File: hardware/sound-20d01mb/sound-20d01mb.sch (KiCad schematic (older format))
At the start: 6 parts

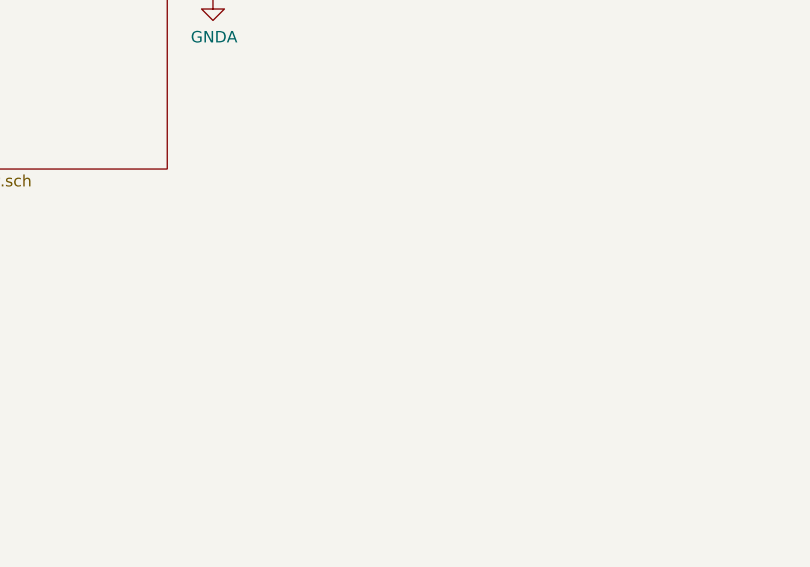
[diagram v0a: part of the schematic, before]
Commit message: Updated power supply unit
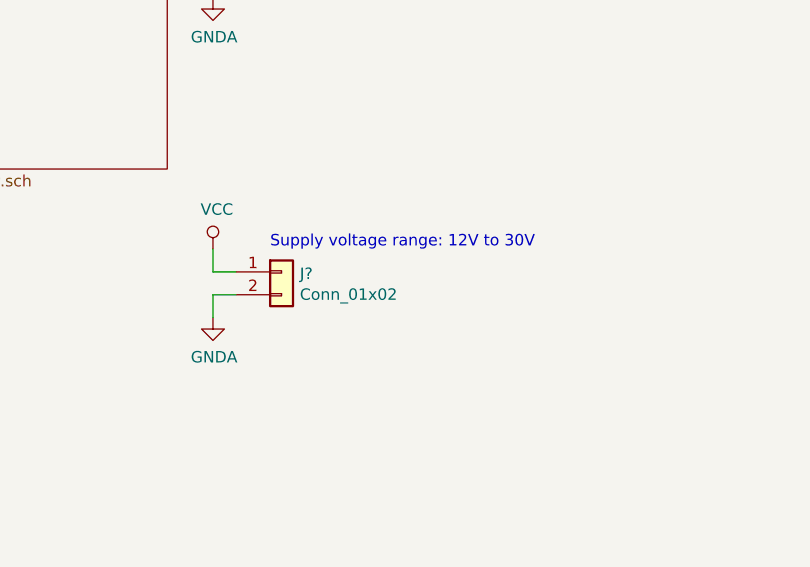
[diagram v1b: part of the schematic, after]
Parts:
- added J?: Conn_01x02, Connector_JST:JST_VH_B2P-VH_1x02_P3.96mm_Vertical, symbol Connector_Generic:Conn_01x02
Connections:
- net GNDA: now also J?.2 (Pin_2)
- new net VCC: J?.1 (Pin_1)
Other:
- note added: "Supply voltage range: 12V to 30V"
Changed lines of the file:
@@
 F1 "psu.sch" 50
 $EndSheet
+$Comp
+L Connector_Generic:Conn_01x02 J?
+U 1 1 60E0FD2A
+P 6150 3400
+F 0 "J?" H 6230 3392 50  0000 L CNN
+F 1 "Conn_01x02" H 6230 3301 50  0000 L CNN
+F 2 "Connector_JST:JST_VH_B2P-VH_1x02_P3.96mm_Vertical" H 6150 3400 50  0001 C CNN
+F 3 "~" H 6150 3400 50  0001 C CNN
+	1    6150 3400
+	1    0    0    -1
+$EndComp
+$Comp
+L power:GNDA #PWR?
+U 1 1 60E0FF3C
+P 5850 3600
+F 0 "#PWR?" H 5850 3350 50  0001 C CNN
+F 1 "GNDA" H 5855 3427 50  0000 C CNN
+F 2 "" H 5850 3600 50  0001 C CNN
+F 3 "" H 5850 3600 50  0001 C CNN
+	1    5850 3600
+	1    0    0    -1
+$EndComp
+Wire Wire Line
+	5950 3500 5850 3500
+Wire Wire Line
+	5850 3500 5850 3600
+$Comp
+L power:VCC #PWR?
+U 1 1 60E100F5
+P 5850 3300
+F 0 "#PWR?" H 5850 3150 50  0001 C CNN
+F 1 "VCC" H 5867 3473 50  0000 C CNN
+F 2 "" H 5850 3300 50  0001 C CNN
+F 3 "" H 5850 3300 50  0001 C CNN
+	1    5850 3300
+	1    0    0    -1
+$EndComp
+Wire Wire Line
+	5950 3400 5850 3400
+Wire Wire Line
+	5850 3400 5850 3300
+Text Notes 6100 3300 0    50   ~ 0
+Supply voltage range: 12V to 30V
 $EndSCHEMATC

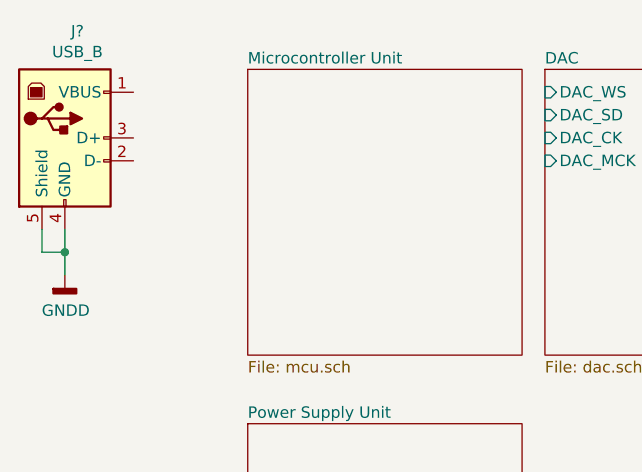
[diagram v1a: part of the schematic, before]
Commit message: Updated MCU schematic
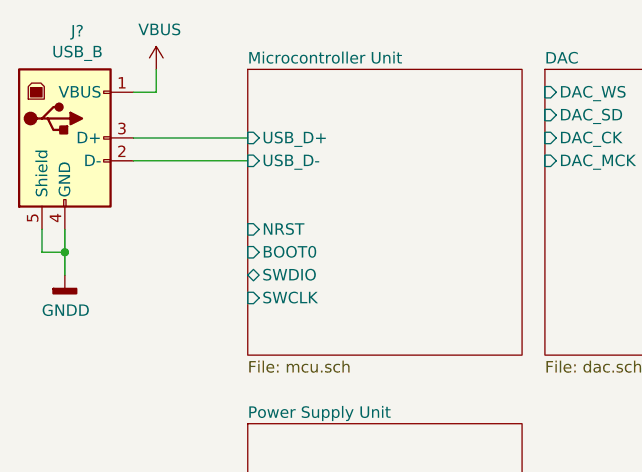
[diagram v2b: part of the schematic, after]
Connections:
- net VBUS: now reaches J?.1 (VBUS)
- net Microcontroller Unit/USB_D-: now reaches J?.2 (D-)
- net Microcontroller Unit/USB_D+: now reaches J?.3 (D+)
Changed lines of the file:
@@
 F0 "Microcontroller Unit" 50
 F1 "mcu.sch" 50
+F2 "USB_D+" I L 1850 2000 50
+F3 "USB_D-" I L 1850 2100 50
+F4 "NRST" I L 1850 2400 50
+F5 "BOOT0" I L 1850 2500 50
+F6 "SWDIO" B L 1850 2600 50
+F7 "SWCLK" I L 1850 2700 50
 $EndSheet
 $Sheet
@@
 Text Notes 6100 3300 0    50   ~ 0
 Supply voltage range: 12V to 30V
+$Comp
+L power:VBUS #PWR?
+U 1 1 60E0D7F5
+P 1450 1700
+F 0 "#PWR?" H 1450 1550 50  0001 C CNN
+F 1 "VBUS" H 1465 1873 50  0000 C CNN
+F 2 "" H 1450 1700 50  0001 C CNN
+F 3 "" H 1450 1700 50  0001 C CNN
+	1    1450 1700
+	1    0    0    -1
+$EndComp
+Wire Wire Line
+	1350 1800 1450 1800
+Wire Wire Line
+	1450 1800 1450 1700
+Wire Wire Line
+	1350 2000 1850 2000
+Wire Wire Line
+	1350 2100 1850 2100
 $EndSCHEMATC

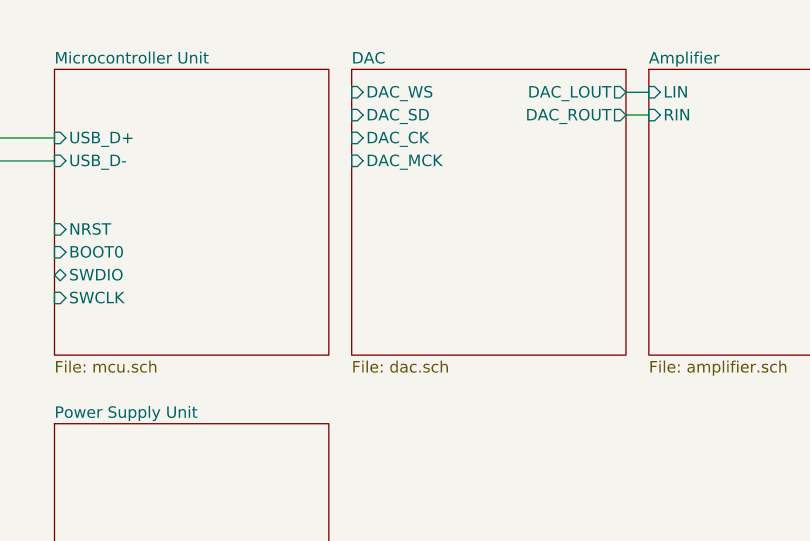
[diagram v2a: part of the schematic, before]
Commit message: Connected MCU to DAC
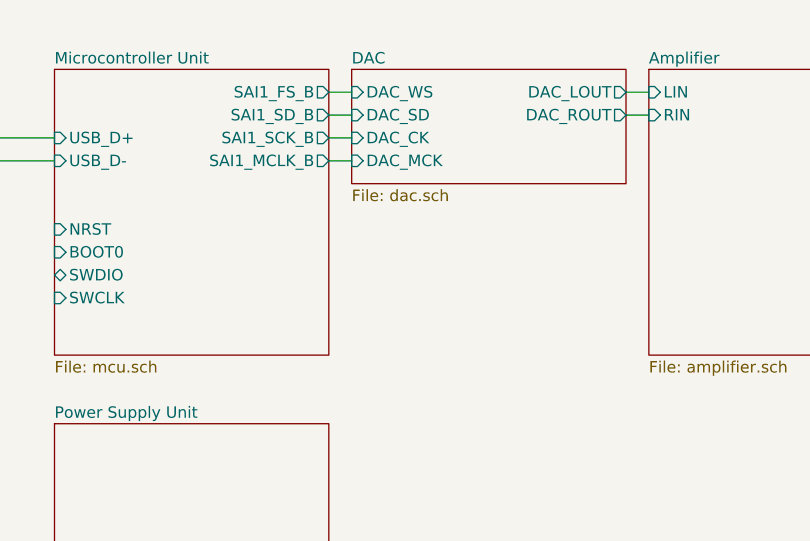
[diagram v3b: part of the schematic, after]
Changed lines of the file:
@@
 F6 "SWDIO" B L 1850 2600 50
 F7 "SWCLK" I L 1850 2700 50
+F8 "SAI1_FS_B" O R 3050 1800 50
+F9 "SAI1_SD_B" O R 3050 1900 50
+F10 "SAI1_SCK_B" O R 3050 2000 50
+F11 "SAI1_MCLK_B" O R 3050 2100 50
 $EndSheet
 $Sheet
-S 3150 1700 1200 1250
+S 3150 1700 1200 500
 U 60DE2DF1
 F0 "DAC" 50
@@
 Wire Wire Line
 	1350 2100 1850 2100
+Wire Wire Line
+	3050 1800 3150 1800
+Wire Wire Line
+	3050 1900 3150 1900
+Wire Wire Line
+	3050 2000 3150 2000
+Wire Wire Line
+	3050 2100 3150 2100
 $EndSCHEMATC

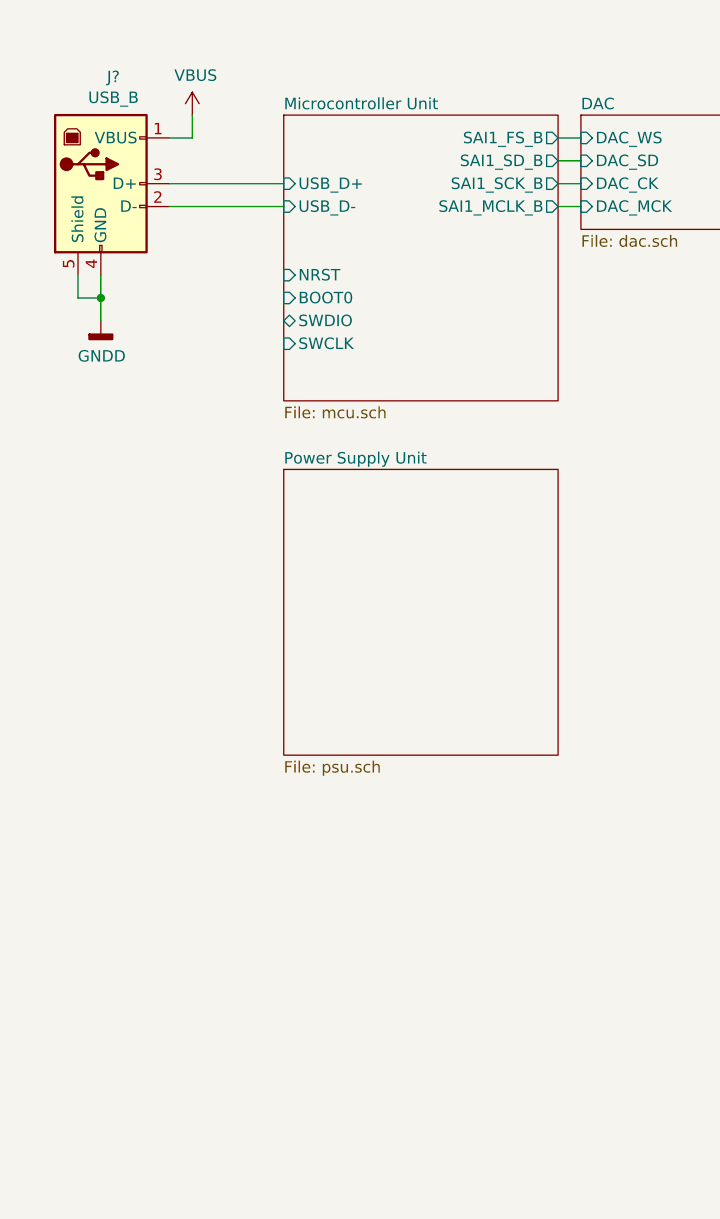
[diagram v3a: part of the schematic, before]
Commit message: Added Debug connector
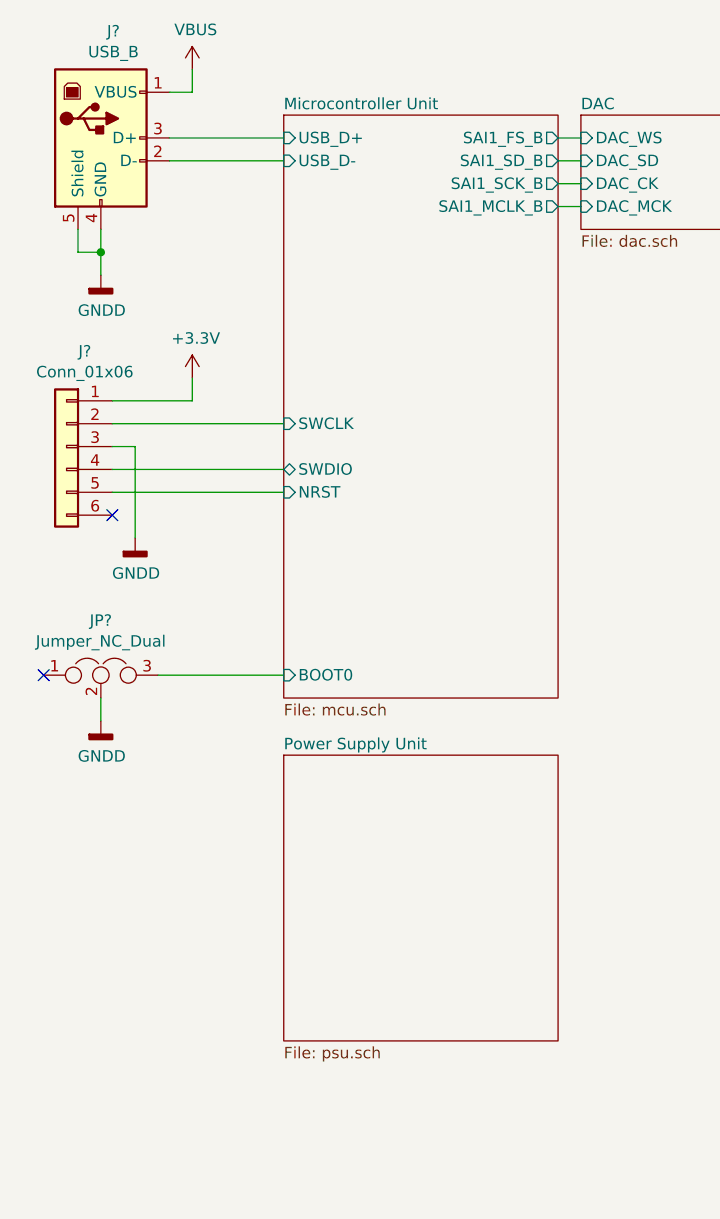
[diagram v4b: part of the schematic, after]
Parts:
- added J?: Conn_01x06, Connector_PinHeader_2.54mm:PinHeader_1x06_P2.54mm_Vertical, symbol Connector_Generic:Conn_01x06
- added JP?: Jumper_NC_Dual, Connector_PinHeader_2.54mm:PinHeader_1x03_P2.54mm_Vertical, symbol Device:Jumper_NC_Dual
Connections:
- net GNDD: now also J?.3 (Pin_3), JP?.2
- net Microcontroller Unit/BOOT0: now also JP?.3
- net Microcontroller Unit/NRST: now also J?.5 (Pin_5)
- net Microcontroller Unit/SWCLK: now also J?.2 (Pin_2)
- net Microcontroller Unit/SWDIO: now also J?.4 (Pin_4)
- new net +3V3: J?.1 (Pin_1)
- no-connect marks 0 -> 2
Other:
- moved on the sheet: J?
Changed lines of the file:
@@
 $EndDescr
 $Sheet
-S 1850 1700 1200 1250
+S 1850 1700 1200 2550
 U 60DE2DEE
 F0 "Microcontroller Unit" 50
 F1 "mcu.sch" 50
-F2 "USB_D+" I L 1850 2000 50
-F3 "USB_D-" I L 1850 2100 50
-F4 "NRST" I L 1850 2400 50
-F5 "BOOT0" I L 1850 2500 50
-F6 "SWDIO" B L 1850 2600 50
-F7 "SWCLK" I L 1850 2700 50
+F2 "USB_D+" I L 1850 1800 50
+F3 "USB_D-" I L 1850 1900 50
+F4 "NRST" I L 1850 3350 50
+F5 "BOOT0" I L 1850 4150 50
+F6 "SWDIO" B L 1850 3250 50
+F7 "SWCLK" I L 1850 3050 50
 F8 "SAI1_FS_B" O R 3050 1800 50
 F9 "SAI1_SD_B" O R 3050 1900 50
@@
 L Connector:USB_B J?
 U 1 1 60E01FED
-P 1050 2000
-F 0 "J?" H 1105 2467 50  0000 C CNN
-F 1 "USB_B" H 1105 2376 50  0000 C CNN
-F 2 "Connector_USB:USB_B_OST_USB-B1HSxx_Horizontal" H 1200 1950 50  0001 C CNN
-F 3 " ~" H 1200 1950 50  0001 C CNN
-	1    1050 2000
+P 1050 1800
+F 0 "J?" H 1105 2267 50  0000 C CNN
+F 1 "USB_B" H 1105 2176 50  0000 C CNN
+F 2 "Connector_USB:USB_B_OST_USB-B1HSxx_Horizontal" H 1200 1750 50  0001 C CNN
+F 3 " ~" H 1200 1750 50  0001 C CNN
+	1    1050 1800
 	1    0    0    -1
 $EndComp
@@
 L power:GNDD #PWR?
 U 1 1 60E023A0
-P 1050 2600
-F 0 "#PWR?" H 1050 2350 50  0001 C CNN
-F 1 "GNDD" H 1054 2445 50  0000 C CNN
-F 2 "" H 1050 2600 50  0001 C CNN
-F 3 "" H 1050 2600 50  0001 C CNN
-	1    1050 2600
-	1    0    0    -1
-$EndComp
-Wire Wire Line
-	1050 2400 1050 2500
-Wire Wire Line
-	950  2400 950  2500
-Wire Wire Line
-	950  2500 1050 2500
-Connection ~ 1050 2500
-Wire Wire Line
-	1050 2500 1050 2600
+P 1050 2400
+F 0 "#PWR?" H 1050 2150 50  0001 C CNN
+F 1 "GNDD" H 1054 2245 50  0000 C CNN
+F 2 "" H 1050 2400 50  0001 C CNN
+F 3 "" H 1050 2400 50  0001 C CNN
+	1    1050 2400
+	1    0    0    -1
+$EndComp
+Wire Wire Line
+	1050 2200 1050 2300
+Wire Wire Line
+	950  2200 950  2300
+Wire Wire Line
+	950  2300 1050 2300
+Connection ~ 1050 2300
+Wire Wire Line
+	1050 2300 1050 2400
 $Comp
 L Connector_Generic:Conn_01x04 J?
@@
 	4350 1900 4450 1900
 $Sheet
-S 1850 3250 1200 1250
+S 1850 4500 1200 1250
 U 61033008
 F0 "Power Supply Unit" 50
@@
 L power:VBUS #PWR?
 U 1 1 60E0D7F5
-P 1450 1700
-F 0 "#PWR?" H 1450 1550 50  0001 C CNN
-F 1 "VBUS" H 1465 1873 50  0000 C CNN
-F 2 "" H 1450 1700 50  0001 C CNN
-F 3 "" H 1450 1700 50  0001 C CNN
-	1    1450 1700
-	1    0    0    -1
-$EndComp
-Wire Wire Line
-	1350 1800 1450 1800
-Wire Wire Line
-	1450 1800 1450 1700
-Wire Wire Line
-	1350 2000 1850 2000
-Wire Wire Line
-	1350 2100 1850 2100
+P 1450 1500
+F 0 "#PWR?" H 1450 1350 50  0001 C CNN
+F 1 "VBUS" H 1465 1673 50  0000 C CNN
+F 2 "" H 1450 1500 50  0001 C CNN
+F 3 "" H 1450 1500 50  0001 C CNN
+	1    1450 1500
+	1    0    0    -1
+$EndComp
+Wire Wire Line
+	1350 1600 1450 1600
+Wire Wire Line
+	1450 1600 1450 1500
+Wire Wire Line
+	1350 1800 1850 1800
+Wire Wire Line
+	1350 1900 1850 1900
 Wire Wire Line
 	3050 1800 3150 1800
@@
 Wire Wire Line
 	3050 2100 3150 2100
+$Comp
+L Connector_Generic:Conn_01x06 J?
+U 1 1 60E2D57C
+P 900 3150
+F 0 "J?" H 820 3567 50  0000 C CNN
+F 1 "Conn_01x06" H 820 3476 50  0000 C CNN
+F 2 "Connector_PinHeader_2.54mm:PinHeader_1x06_P2.54mm_Vertical" H 900 3150 50  0001 C CNN
+F 3 "~" H 900 3150 50  0001 C CNN
+	1    900  3150
+	-1   0    0    -1
+$EndComp
+$Comp
+L Device:Jumper_NC_Dual JP?
+U 1 1 60E2D95F
+P 1050 4150
+F 0 "JP?" H 1050 4389 50  0000 C CNN
+F 1 "Jumper_NC_Dual" H 1050 4298 50  0000 C CNN
+F 2 "Connector_PinHeader_2.54mm:PinHeader_1x03_P2.54mm_Vertical" H 1050 4150 50  0001 C CNN
+F 3 "~" H 1050 4150 50  0001 C CNN
+	1    1050 4150
+	1    0    0    -1
+$EndComp
+NoConn ~ 1100 3450
+NoConn ~ 800  4150
+Wire Wire Line
+	1100 3050 1850 3050
+$Comp
+L power:+3.3V #PWR?
+U 1 1 60E2E997
+P 1450 2850
+F 0 "#PWR?" H 1450 2700 50  0001 C CNN
+F 1 "+3.3V" H 1465 3023 50  0000 C CNN
+F 2 "" H 1450 2850 50  0001 C CNN
+F 3 "" H 1450 2850 50  0001 C CNN
+	1    1450 2850
+	1    0    0    -1
+$EndComp
+Wire Wire Line
+	1100 2950 1450 2950
+Wire Wire Line
+	1450 2950 1450 2850
+$Comp
+L power:GNDD #PWR?
+U 1 1 60E2EDAD
+P 1200 3550
+F 0 "#PWR?" H 1200 3300 50  0001 C CNN
+F 1 "GNDD" H 1204 3395 50  0000 C CNN
+F 2 "" H 1200 3550 50  0001 C CNN
+F 3 "" H 1200 3550 50  0001 C CNN
+	1    1200 3550
+	1    0    0    -1
+$EndComp
+Wire Wire Line
+	1100 3150 1200 3150
+Wire Wire Line
+	1200 3150 1200 3550
+Wire Wire Line
+	1100 3250 1850 3250
+Wire Wire Line
+	1100 3350 1850 3350
+$Comp
+L power:GNDD #PWR?
+U 1 1 60E30724
+P 1050 4350
+F 0 "#PWR?" H 1050 4100 50  0001 C CNN
+F 1 "GNDD" H 1054 4195 50  0000 C CNN
+F 2 "" H 1050 4350 50  0001 C CNN
+F 3 "" H 1050 4350 50  0001 C CNN
+	1    1050 4350
+	1    0    0    -1
+$EndComp
+Wire Wire Line
+	1050 4250 1050 4350
+Wire Wire Line
+	1300 4150 1850 4150
 $EndSCHEMATC

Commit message: Updated sound-20d01mb.sch
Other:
- note added: "Debug connector"
- note added: "USB 2.0"
- moved on the sheet: H?, J?, JP?

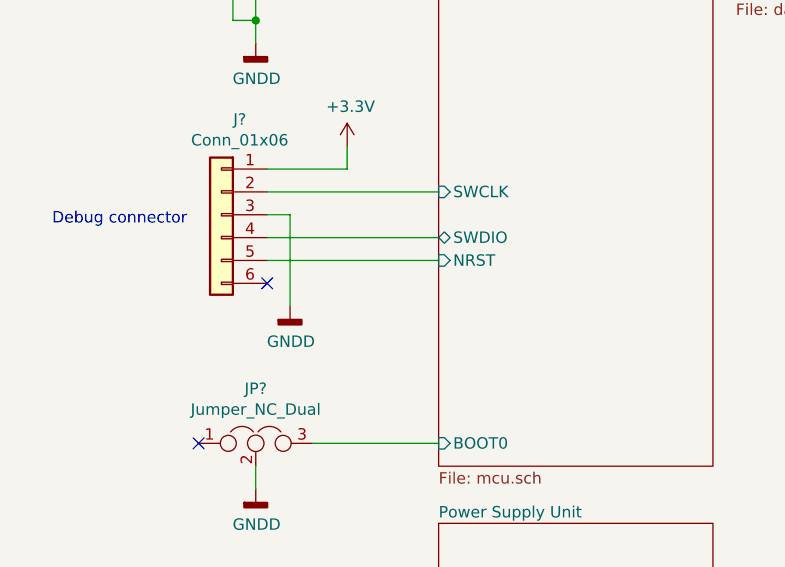
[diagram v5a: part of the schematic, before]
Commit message: Added SWO
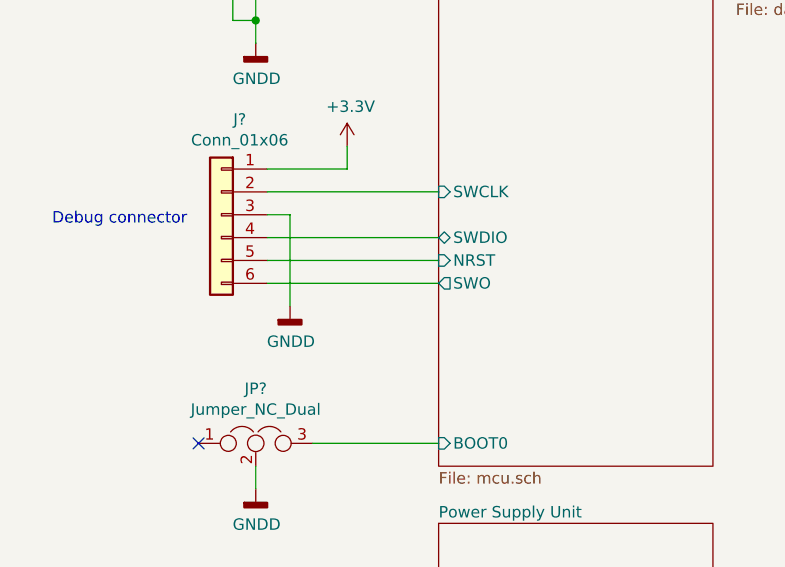
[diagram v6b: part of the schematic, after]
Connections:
- net Microcontroller Unit/SWO: now reaches J?.6 (Pin_6)
- no-connect marks 2 -> 1
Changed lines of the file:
@@
 F10 "SAI1_SCK_B" O R 3650 2000 50
 F11 "SAI1_MCLK_B" O R 3650 2100 50
+F12 "SWO" O L 2450 3450 50
 $EndSheet
 $Sheet
@@
 	1    0    0    -1
 $EndComp
-NoConn ~ 1700 3450
 NoConn ~ 1400 4150
 Wire Wire Line
@@
 Text Notes 1350 1800 2    50   ~ 0
 USB 2.0
+Wire Wire Line
+	1700 3450 2450 3450
 $EndSCHEMATC
